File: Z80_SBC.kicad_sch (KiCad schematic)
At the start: 10 parts, among them U1 Z80CPU, U2 HM62256BLP, U3 27C64, U4 74HCT04, U5 74LS139, Y1 1.8432MHz

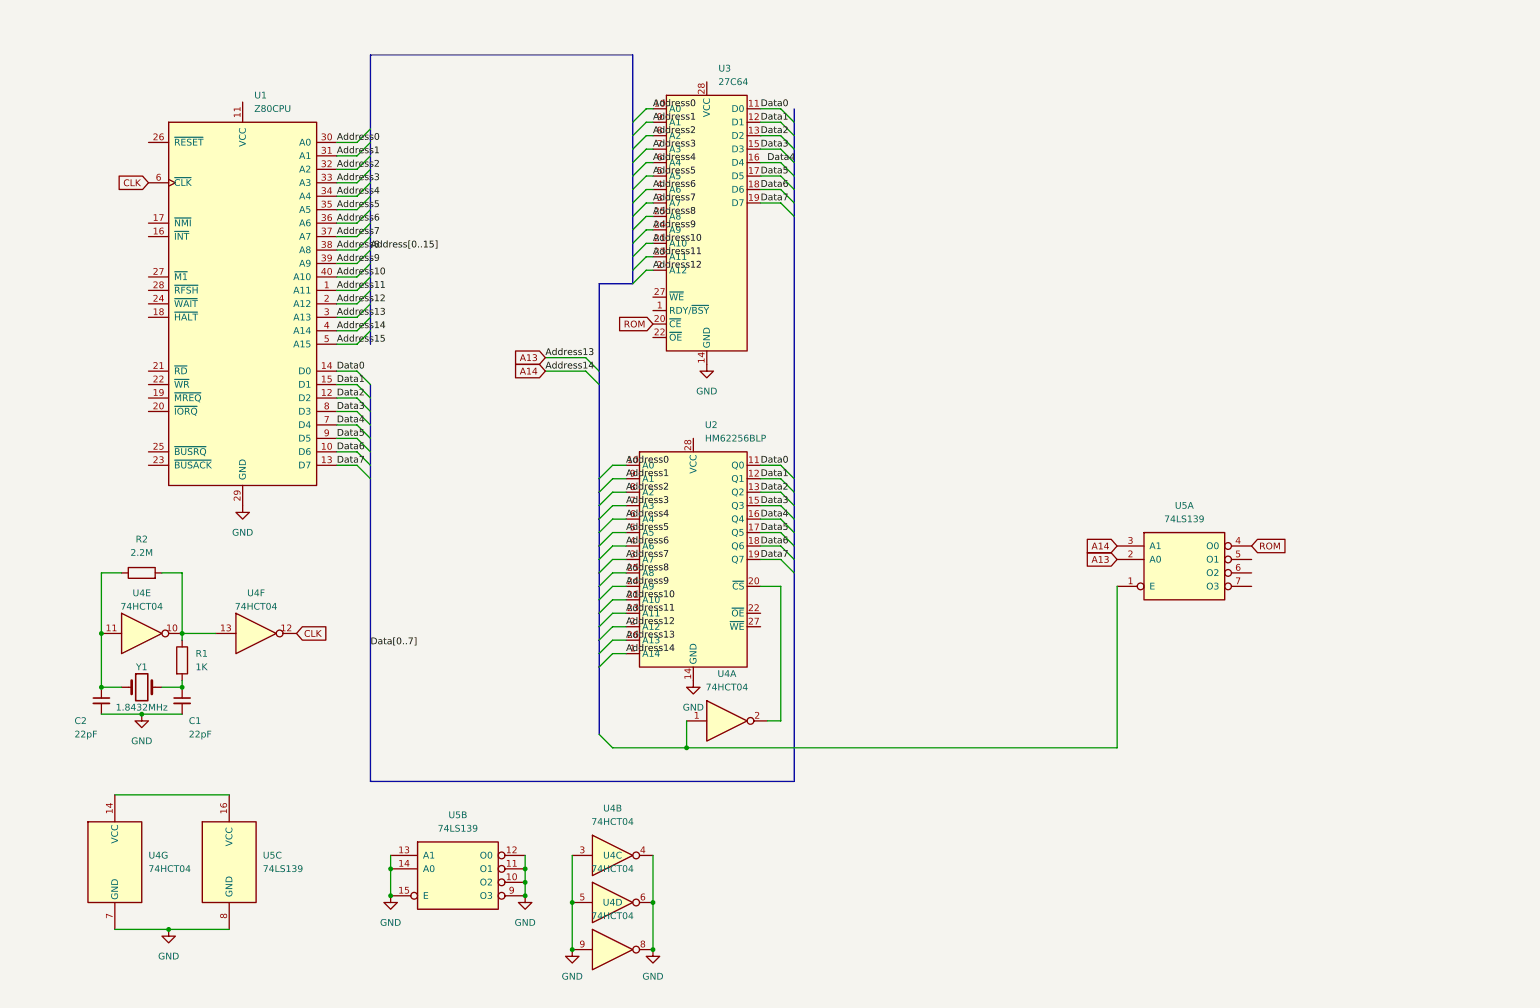
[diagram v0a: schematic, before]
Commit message: added 6850 USART
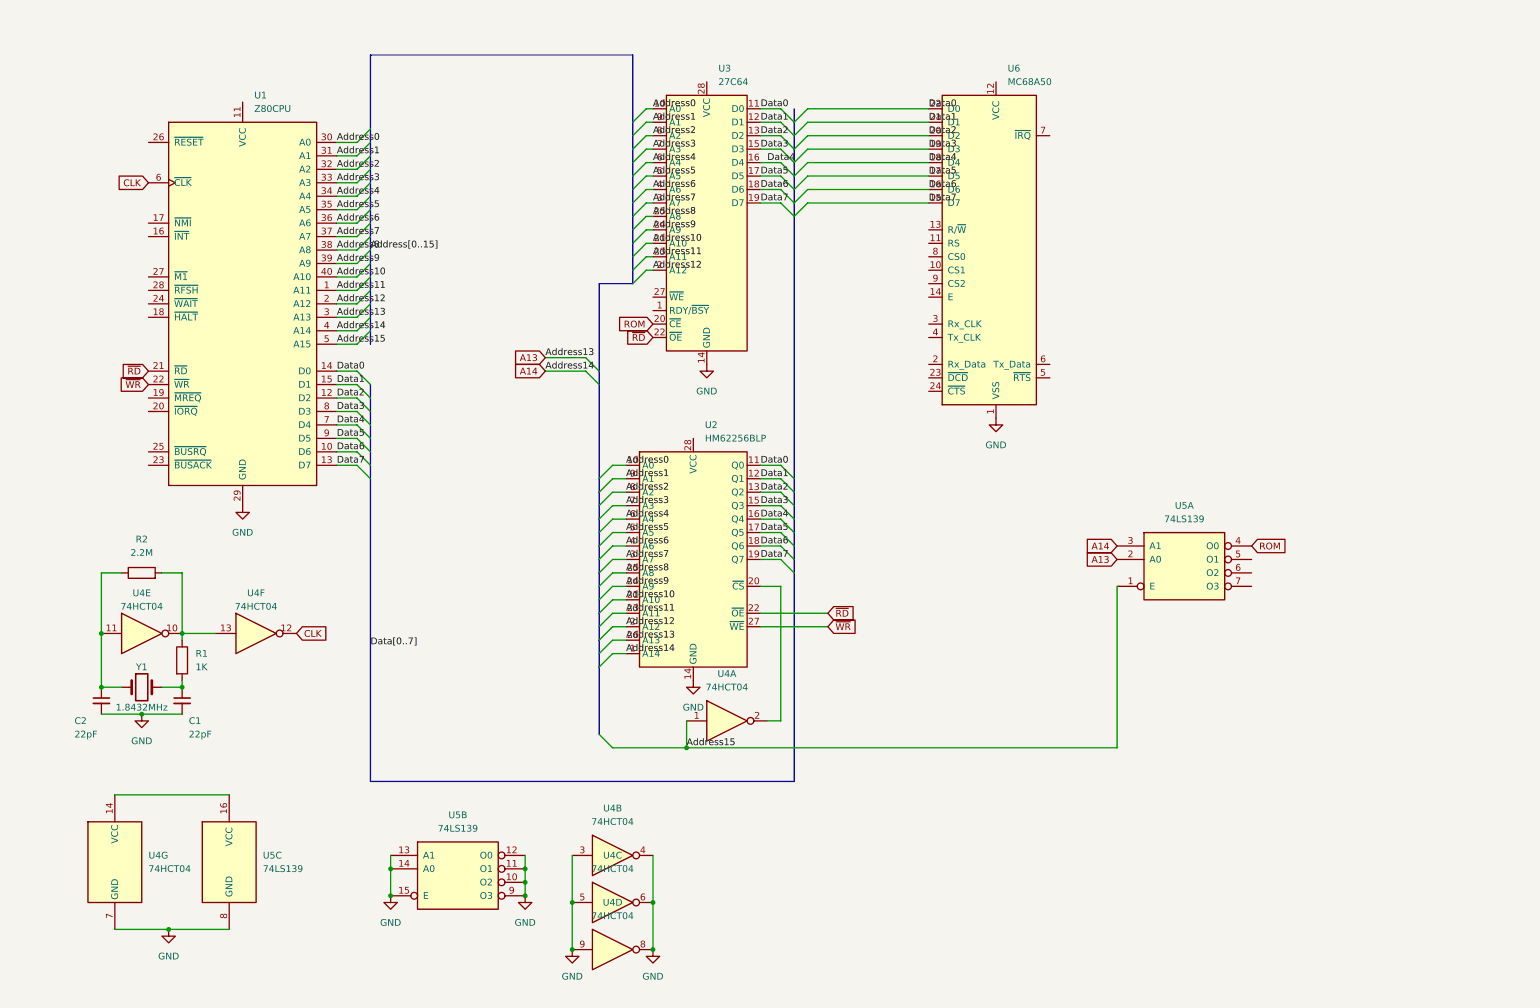
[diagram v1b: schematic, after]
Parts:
- added U6: MC68A50, Package_DIP:DIP-40_W15.24mm, symbol Interface_UART:MC68A50
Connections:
- net Address15: now also U4.1, U5.1 (E)
- net Data0: now also U6.22 (D0)
- net Data1: now also U6.21 (D1)
- net Data2: now also U6.20 (D2)
- net Data3: now also U6.19 (D3)
- net Data4: now also U6.18 (D4)
- net Data5: now also U6.17 (D5)
- net Data6: now also U6.16 (D6)
- net Data7: now also U6.15 (D7)
- net GND: now also U6.1 (VSS)
- net ~{RD}: now reaches U1.21 (~{RD})
- net ~{RD}: now also U2.22 (~{OE}), U3.22 (~{OE})
- net ~{WR}: now reaches U1.22 (~{WR})
- net ~{WR}: now also U2.27 (~{WE})

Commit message: poor route
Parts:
- added C10, C11, C4, C5, C6, C7, C8, C9: 0.1uF, Capacitor_THT:C_Radial_D4.0mm_H5.0mm_P1.50mm, symbol Device:C_Small
- added C3: 100uF, Capacitor_THT:CP_Radial_D4.0mm_P1.50mm, symbol Device:C_Small
- added D1, D2, D3, D4, D5, D6, D7, D8: LED, LED_THT:LED_D3.0mm, symbol Device:LED
- added J1: USB_C_Receptacle_PowerOnly_6P, Connector_USB:USB_C_Receptacle_GCT_USB4125-xx-x_6P_TopMnt_Horizontal, symbol Connector:USB_C_Receptacle_PowerOnly_6P
- added J2: Conn_01x04_Pin, Connector_PinHeader_1.27mm:PinHeader_1x04_P1.27mm_Vertical, symbol Connector:Conn_01x04_Pin
- added R4: 3k3, Resistor_THT:R_Axial_DIN0309_L9.0mm_D3.2mm_P12.70mm_Horizontal, symbol Device:R_Small
- added RN1: R_Network08, Resistor_THT:R_Array_SIP9, symbol Device:R_Network08
- added U7: 74LS573, Package_DIP:DIP-20_W7.62mm, symbol 74xx:74LS573
- added U8: 74LS32, Package_DIP:DIP-14_W7.62mm, symbol 74xx:74LS32
- U6: footprint Package_DIP:DIP-40_W15.24mm -> Package_DIP:DIP-24_W15.24mm
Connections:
- net Address0 is gone; now on net A0: U1.30 (A0), U2.10 (A0), U3.10 (A0)
- net Address6 is gone; now on net A6: U1.36 (A6), U2.4 (A6), U3.4 (A6)
- net Address7 is gone; now on net A7: U1.37 (A7), U2.3 (A7), U3.3 (A7)
- net CLK: now also U6.3 (Rx_CLK), U6.4 (Tx_CLK)
- net Data0: now also U7.2 (D0)
- net Data1: now also U7.3 (D1)
- net Data2: now also U7.4 (D2)
- net Data3: now also U7.5 (D3)
- net Data4: now also U7.6 (D4)
- net Data5: now also U7.7 (D5)
- net Data6: now also U7.8 (D6)
- net Data7: now also U7.9 (D7)
- net GND: now also U6.23 (~{DCD}), U6.24 (~{CTS}), C10.2, C11.2, C3.2, C4.2, C5.2, C6.2, C7.2, C8.2, C9.2, J1.A12 (GND), J1.A5 (CC1), J1.B12 (GND), J1.B5 (CC2), J1.S1 (SHIELD), J2.1 (Pin_1), RN1.1 (common), U7.1 (OE), U7.10 (GND), U8.1, U8.2, U8.3, U8.4, U8.5, U8.6, U8.7 (GND); no longer U4.3, U4.4, U4.5, U4.6
- net ~{RD}: now also U8.9; no longer U2.22 (~{OE}), U3.22 (~{OE})
- net ~{WR}: now also U6.13 (R/~{W}), U8.13; no longer U2.27 (~{WE})
- net A6: now reaches U6.10 (CS1)
- net A0: now reaches U6.11 (RS)
- net 5V: now reaches U6.12 (VCC)
- net 5V: now also U1.11 (VCC), U1.17 (~{NMI}), U1.24 (~{WAIT}), U1.25 (~{BUSRQ}), U2.28 (VCC), U3.27 (~{WE}), U3.28 (VCC), U4.14 (VCC), U5.16 (VCC), C10.1, C11.1, C3.1, C4.1, C5.1, C6.1, C7.1, C8.1, C9.1, J1.A9 (VBUS), J1.B9 (VBUS), J2.4 (Pin_4), R4.1, U7.20 (VCC), U8.14 (VCC)
- net at U6.14 (E): now also U4.4
- net RX: now reaches U6.2 (Rx_Data)
- net RX: now also J2.3 (Pin_3)
- net TX: now reaches U6.6 (Tx_Data)
- net TX: now also J2.2 (Pin_2)
- net ~{INT}: now reaches U6.7 (~{IRQ})
- net ~{INT}: now also U1.16 (~{INT}), R4.2
- net ~{M1}: now reaches U6.8 (CS0)
- net ~{M1}: now also U1.27 (~{M1})
- net A7: now reaches U6.9 (CS2)
- net ~{MREQ}: now reaches U1.19 (~{MREQ})
- net ~{MREQ}: now also U8.10, U8.12
- net ~{I/O}: now reaches U1.20 (~{IORQ})
- net ~{I/O}: now also U4.3
- net at U5.5 (O1): now also U4.5
- new net: D1.1 (K), RN1.9 (R8)
- new net: D1.2 (A), U7.12 (Q7)
- new net: D3.1 (K), RN1.7 (R6)
- new net: D3.2 (A), U7.14 (Q5)
- new net: D8.1 (K), RN1.2 (R1)
- new net: D8.2 (A), U7.19 (Q0)
- new net: U4.6, U7.11 (Load)
- new net: D5.1 (K), RN1.5 (R4)
- new net: D5.2 (A), U7.16 (Q3)
- new net: D4.1 (K), RN1.6 (R5)
- new net: D4.2 (A), U7.15 (Q4)
- new net: D7.1 (K), RN1.3 (R2)
- new net: D6.1 (K), RN1.4 (R3)
- new net: D2.1 (K), RN1.8 (R7)
- new net: D2.2 (A), U7.13 (Q6)
- new net: D6.2 (A), U7.17 (Q2)
- new net: D7.2 (A), U7.18 (Q1)
- new net ~{MEMRD}: U2.22 (~{OE}), U3.22 (~{OE}), U8.8
- new net ~{MEMWR}: U2.27 (~{WE}), U8.11
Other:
- moved on the sheet: U4B, U4C, U5A, U5B

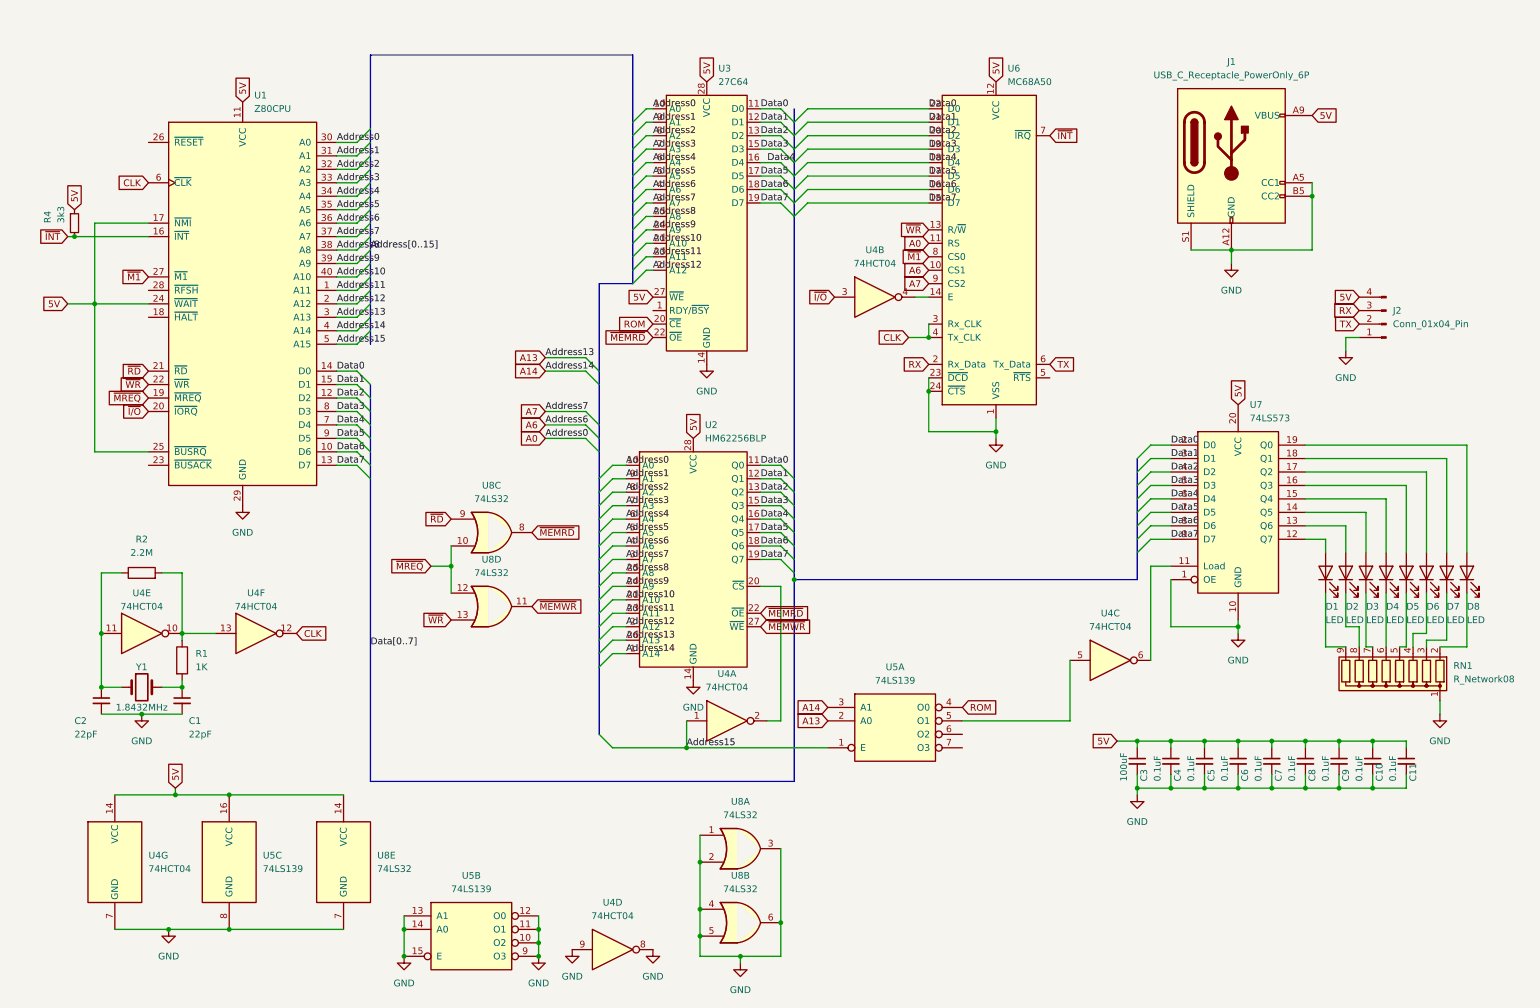
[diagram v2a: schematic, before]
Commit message: fix DRC errors and warning, add reset and power
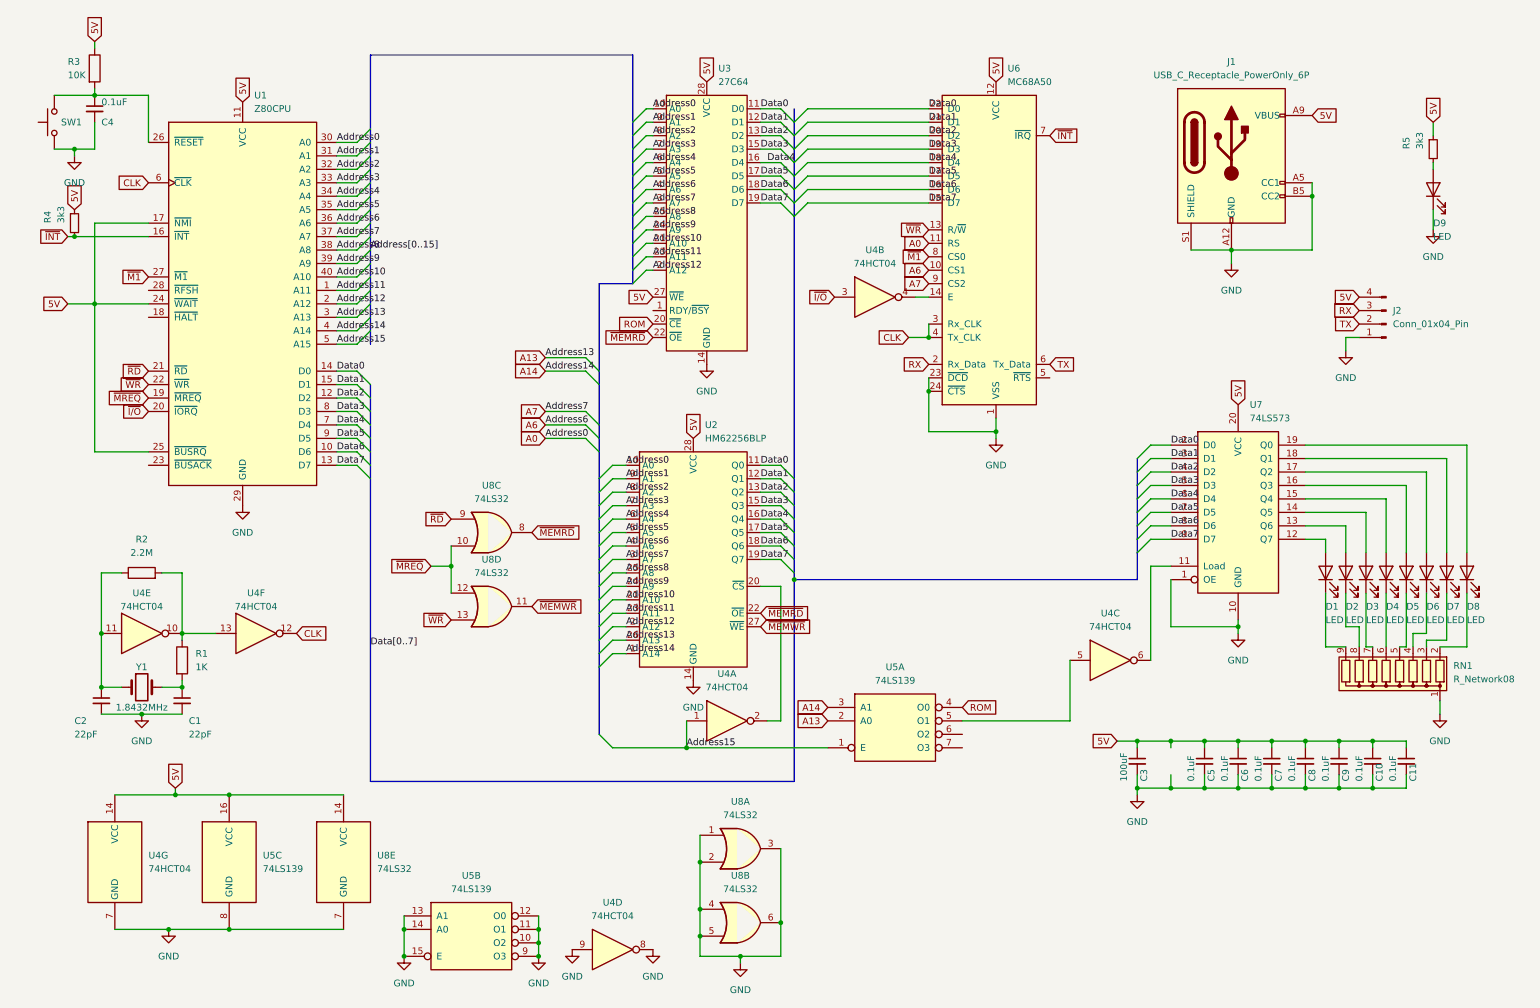
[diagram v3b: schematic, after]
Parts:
- added D9: LED, LED_THT:LED_D3.0mm, symbol Device:LED
- added R3: 10K, Resistor_THT:R_Axial_DIN0309_L9.0mm_D3.2mm_P12.70mm_Horizontal, symbol Device:R
- added R5: 3k3, Resistor_THT:R_Axial_DIN0309_L9.0mm_D3.2mm_P12.70mm_Horizontal, symbol Device:R_Small
- added SW1: SW_Push, Button_Switch_THT:SW_PUSH_6mm, symbol Switch:SW_Push
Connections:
- net 5V: now also R3.1, R5.1; no longer C4.1
- net GND: now also D9.1 (K), SW1.1
- net at U1.26 (~{RESET}): now also C4.1, R3.2, SW1.2
- new net: D9.2 (A), R5.2
